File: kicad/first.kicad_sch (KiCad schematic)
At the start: 100 parts, among them J1 Conn_01x04_Pin, P1 USB_C_Plug_USB2.0, Q1 MMUN2111LT1G, Q2 MMBT3904, Q3 MMUN2111LT1G, Q4 MMBT3904, SW1 SW_SPDT, SW2 RotaryEncoder_Switch_MP, SW3 RotaryEncoder_Switch_MP, SW4 RotaryEncoder_Switch_MP, U1 OPA1678, U1 STM32F407VETx, U2 OPA1678, U3 CS4272, U3 OPA1678, U4 TPS7A20xxxDBV, Y1 16 MHz

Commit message: um
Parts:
- removed C20: 47u, symbol Device:C
- added C20: 47u, symbol Device:C_Polarized
- added C44: 100n/50V+, symbol Device:C
- C14: value 1u -> 1u /10V
- C15: value 1u -> 1u/10V
- C22: value 1u -> 1u/10V+
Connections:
- net GND: now also C20.2, C44.2
- net VQ1: now also C44.1
- net at C21.1, U3.22 (FILT+): now also C20.1
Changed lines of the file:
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@@
 	)
 	(junction
+		(at 372.11 140.97)
+		(diameter 0)
+		(color 0 0 0 0)
+	)
+	(junction
 		(at 181.61 33.02)
 		(diameter 0)
@@
 	)
 	(junction
-		(at 349.25 143.51)
-		(diameter 0)
-		(color 0 0 0 0)
-	)
-	(junction
 		(at 121.92 114.3)
 		(diameter 0)
@@
 	)
 	(junction
+		(at 349.25 143.51)
+		(diameter 0)
+		(color 0 0 0 0)
+	)
+	(junction
 		(at 300.99 83.82)
 		(diameter 0)
@@
 	(wire
 		(pts
+			(xy 372.11 140.97) (xy 387.35 140.97)
+		)
+		(stroke
+			(width 0)
+			(type default)
+		)
+	)
+	(wire
+		(pts
 			(xy 158.75 271.78) (xy 158.75 273.05)
 		)
@@
 	(wire
 		(pts
+			(xy 387.35 142.24) (xy 387.35 140.97)
+		)
+		(stroke
+			(width 0)
+			(type default)
+		)
+	)
+	(wire
+		(pts
 			(xy 229.87 181.61) (xy 229.87 182.88)
 		)
@@
 	(wire
 		(pts
+			(xy 387.35 149.86) (xy 387.35 151.13)
+		)
+		(stroke
+			(width 0)
+			(type default)
+		)
+	)
+	(wire
+		(pts
 			(xy 336.55 223.52) (xy 328.93 223.52)
 		)
@@
 	(wire
 		(pts
+			(xy 387.35 151.13) (xy 372.11 151.13)
+		)
+		(stroke
+			(width 0)
+			(type default)
+		)
+	)
+	(wire
+		(pts
 			(xy 269.24 234.95) (xy 293.37 234.95)
 		)
@@
 	(wire
 		(pts
-			(xy 349.25 143.51) (xy 360.68 143.51)
-		)
-		(stroke
-			(width 0)
-			(type default)
-		)
-	)
-	(wire
-		(pts
 			(xy 300.99 148.59) (xy 304.8 148.59)
 		)
@@
 	(wire
 		(pts
+			(xy 349.25 143.51) (xy 360.68 143.51)
+		)
+		(stroke
+			(width 0)
+			(type default)
+		)
+	)
+	(wire
+		(pts
 			(xy 293.37 234.95) (xy 321.31 234.95)
 		)
@@
 	(symbol
 		(lib_id "Device:C")
+		(at 387.35 146.05 0)
+		(unit 1)
+		(body_style 1)
+		(exclude_from_sim no)
+		(in_bom yes)
+		(on_board yes)
+		(in_pos_files yes)
+		(dnp no)
+		(fields_autoplaced yes)
+		(property "Reference" "C44"
+			(at 391.16 144.7799 0)
+			(show_name no)
+			(do_not_autoplace no)
+			(effects
+				(font
+					(size 1.27 1.27)
+				)
+				(justify left)
+			)
+		)
+		(property "Value" "100n/50V+"
+			(at 391.16 147.3199 0)
+			(show_name no)
+			(do_not_autoplace no)
+			(effects
+				(font
+					(size 1.27 1.27)
+				)
+				(justify left)
+			)
+		)
+		(property "Footprint" ""
+			(at 388.3152 149.86 0)
+			(hide yes)
+			(show_name no)
+			(do_not_autoplace no)
+			(effects
+				(font
+					(size 1.27 1.27)
+				)
+			)
+		)
+		(property "Datasheet" ""
+			(at 387.35 146.05 0)
+			(hide yes)
+			(show_name no)
+			(do_not_autoplace no)
+			(effects
+				(font
+					(size 1.27 1.27)
+				)
+			)
+		)
+		(property "Description" "Unpolarized capacitor"
+			(at 387.35 146.05 0)
+			(hide yes)
+			(show_name no)
+			(do_not_autoplace no)
+			(effects
+				(font
+					(size 1.27 1.27)
+				)
+			)
+		)
+		(pin "1"
+		)
+		(pin "2"
+		)
+		(instances
+			(project "first"
+				(path "/580becc7-fa47-4b4d-a43e-4b9316967eb7"
+					(reference "C44")
+					(unit 1)
+				)
+			)
+		)
+	)
+	(symbol
+		(lib_id "Device:C")
 		(at 59.69 261.62 270)
 		(unit 1)
@@
 			)
 		)
-		(property "Value" "1u"
+		(property "Value" "1u /10V"
 			(at 326.898 34.036 0)
 			(show_name no)
@@
 	)
 	(symbol
+		(lib_id "Device:C_Polarized")
+		(at 349.25 147.32 0)
+		(unit 1)
+		(body_style 1)
+		(exclude_from_sim no)
+		(in_bom yes)
+		(on_board yes)
+		(in_pos_files yes)
+		(dnp no)
+		(fields_autoplaced yes)
+		(property "Reference" "C20"
+			(at 353.06 145.1609 0)
+			(show_name no)
+			(do_not_autoplace no)
+			(effects
+				(font
+					(size 1.27 1.27)
+				)
+				(justify left)
+			)
+		)
+		(property "Value" "47u"
+			(at 353.06 147.7009 0)
+			(show_name no)
+			(do_not_autoplace no)
+			(effects
+				(font
+					(size 1.27 1.27)
+				)
+				(justify left)
+			)
+		)
+		(property "Footprint" ""
+			(at 350.2152 151.13 0)
+			(hide yes)
+			(show_name no)
+			(do_not_autoplace no)
+			(effects
+				(font
+					(size 1.27 1.27)
+				)
+			)
+		)
+		(property "Datasheet" ""
+			(at 349.25 147.32 0)
+			(hide yes)
+			(show_name no)
+			(do_not_autoplace no)
+			(effects
+				(font
+					(size 1.27 1.27)
+				)
+			)
+		)
+		(property "Description" "Polarized capacitor"
+			(at 349.25 147.32 0)
+			(hide yes)
+			(show_name no)
+			(do_not_autoplace no)
+			(effects
+				(font
+					(size 1.27 1.27)
+				)
+			)
+		)
+		(pin "1"
+		)
+		(pin "2"
+		)
+		(instances
+			(project "first"
+				(path "/580becc7-fa47-4b4d-a43e-4b9316967eb7"
+					(reference "C20")
+					(unit 1)
+				)
+			)
+		)
+	)
+	(symbol
 		(lib_id "Amplifier_Operational:NE5532")
 		(at 87.63 240.03 0)
@@
 			)
 		)
-		(property "Value" "1u"
+		(property "Value" "1u/10V"
 			(at 358.14 33.0199 0)
 			(show_name no)
@@
 	)
 	(symbol
-		(lib_id "Device:C")
-		(at 349.25 147.32 0)
-		(unit 1)
-		(body_style 1)
-		(exclude_from_sim no)
-		(in_bom yes)
-		(on_board yes)
-		(in_pos_files yes)
-		(dnp no)
-		(fields_autoplaced yes)
-		(property "Reference" "C20"
-			(at 353.06 146.0499 0)
-			(show_name no)
-			(do_not_autoplace no)
-			(effects
-				(font
-					(size 1.27 1.27)
-				)
-				(justify left)
-			)
-		)
-		(property "Value" "47u"
-			(at 353.06 148.5899 0)
-			(show_name no)
-			(do_not_autoplace no)
-			(effects
-				(font
-					(size 1.27 1.27)
-				)
-				(justify left)
-			)
-		)
-		(property "Footprint" ""
-			(at 350.2152 151.13 0)
-			(hide yes)
-			(show_name no)
-			(do_not_autoplace no)
-			(effects
-				(font
-					(size 1.27 1.27)
-				)
-			)
-		)
-		(property "Datasheet" ""
-			(at 349.25 147.32 0)
-			(hide yes)
-			(show_name no)
-			(do_not_autoplace no)
-			(effects
-				(font
-					(size 1.27 1.27)
-				)
-			)
-		)
-		(property "Description" "Unpolarized capacitor"
-			(at 349.25 147.32 0)
-			(hide yes)
-			(show_name no)
-			(do_not_autoplace no)
-			(effects
-				(font
-					(size 1.27 1.27)
-				)
-			)
-		)
-		(pin "2"
-		)
-		(pin "1"
-		)
-		(instances
-			(project "first"
-				(path "/580becc7-fa47-4b4d-a43e-4b9316967eb7"
-					(reference "C20")
-					(unit 1)
-				)
-			)
-		)
-	)
-	(symbol
 		(lib_id "Connector:Conn_01x04_Pin")
 		(at 302.26 99.06 0)
@@
 			)
 		)
-		(property "Value" "1u"
+		(property "Value" "1u/10V+"
 			(at 375.92 147.3199 0)
 			(show_name no)

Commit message: some cleanup, output audio connectors, some capacitor changes at input buffer and preamp
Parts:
- removed C23, C24: 10u, symbol Device:C_Polarized
- added C24, C25: 47n, symbol Device:C
- C23: renamed from C44; value 100n/50V+ -> 100n
- renumbered C25 to C26, C26 to C27, C27 to C28, C28 to C29, C29 to C30, C30 to C31, C31 to C32, C32 to C33, C33 to C34, C34 to C35, C35 to C36, C36 to C37, C37 to C38, C38 to C39, C39 to C40, C40 to C41
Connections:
- net Inputs/AIN_L: now also C24.2
- net Inputs/AIN_R: now also C25.2
- net at R5.2, U1.5 (+): now also C25.1
- net at R4.1, U1.3 (+): now also C24.1
- net AOUTA renamed AOUT_L
- net AOUTB renamed AOUT_R

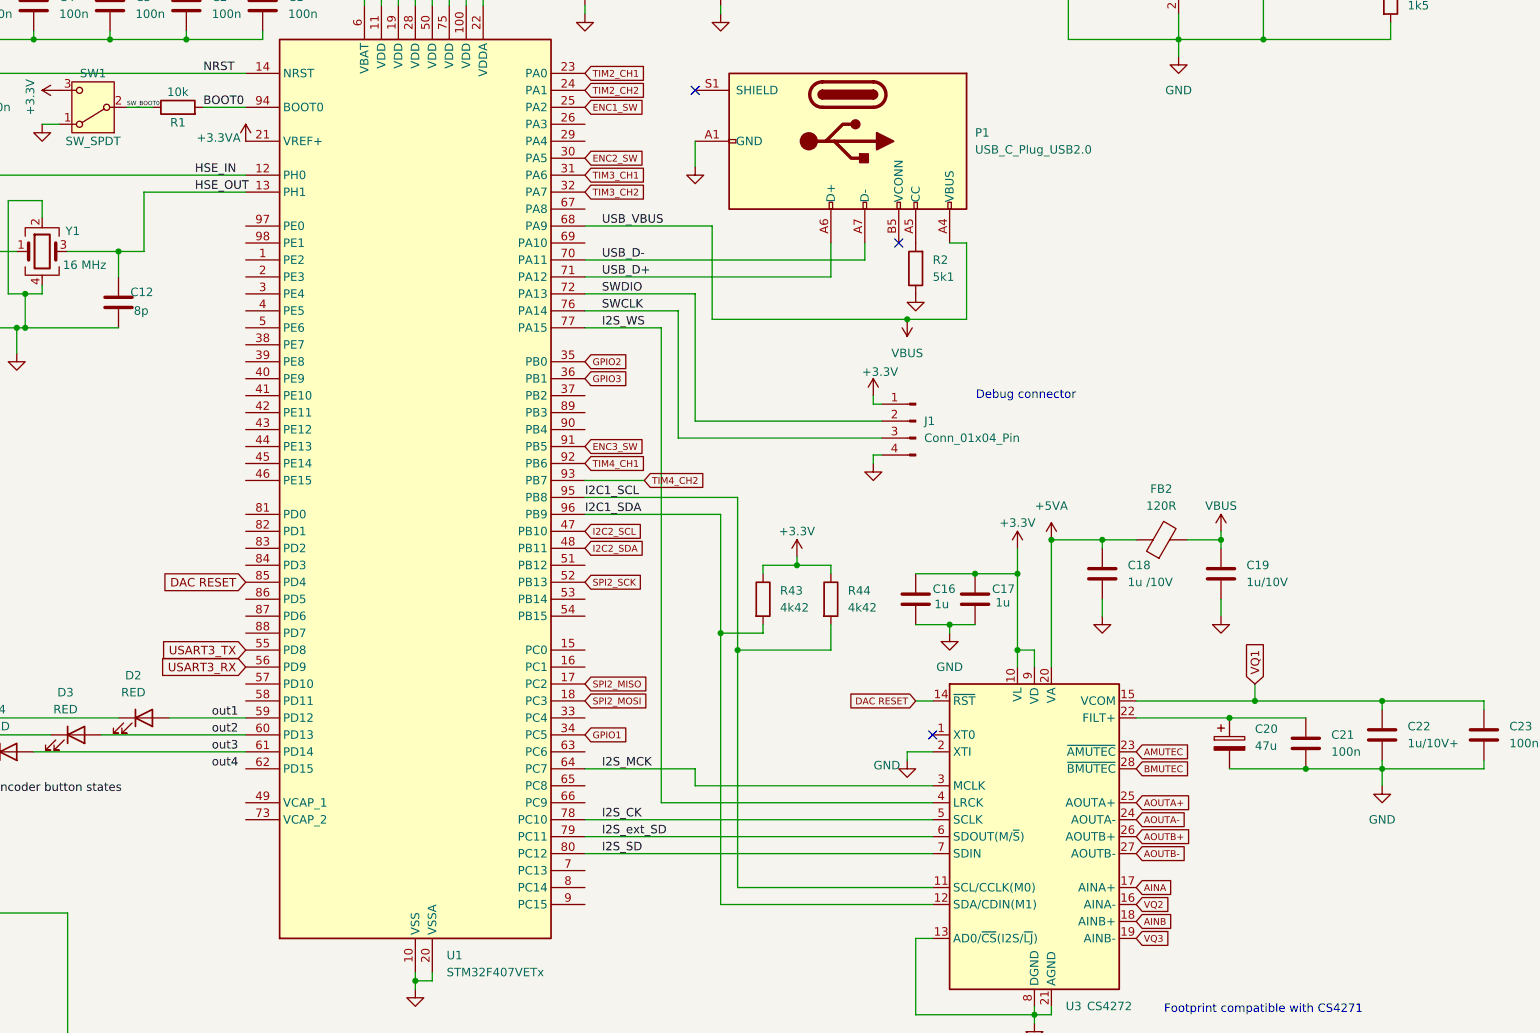
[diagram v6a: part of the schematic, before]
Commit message: extra pin header, VCAP capacitors, no connect flags
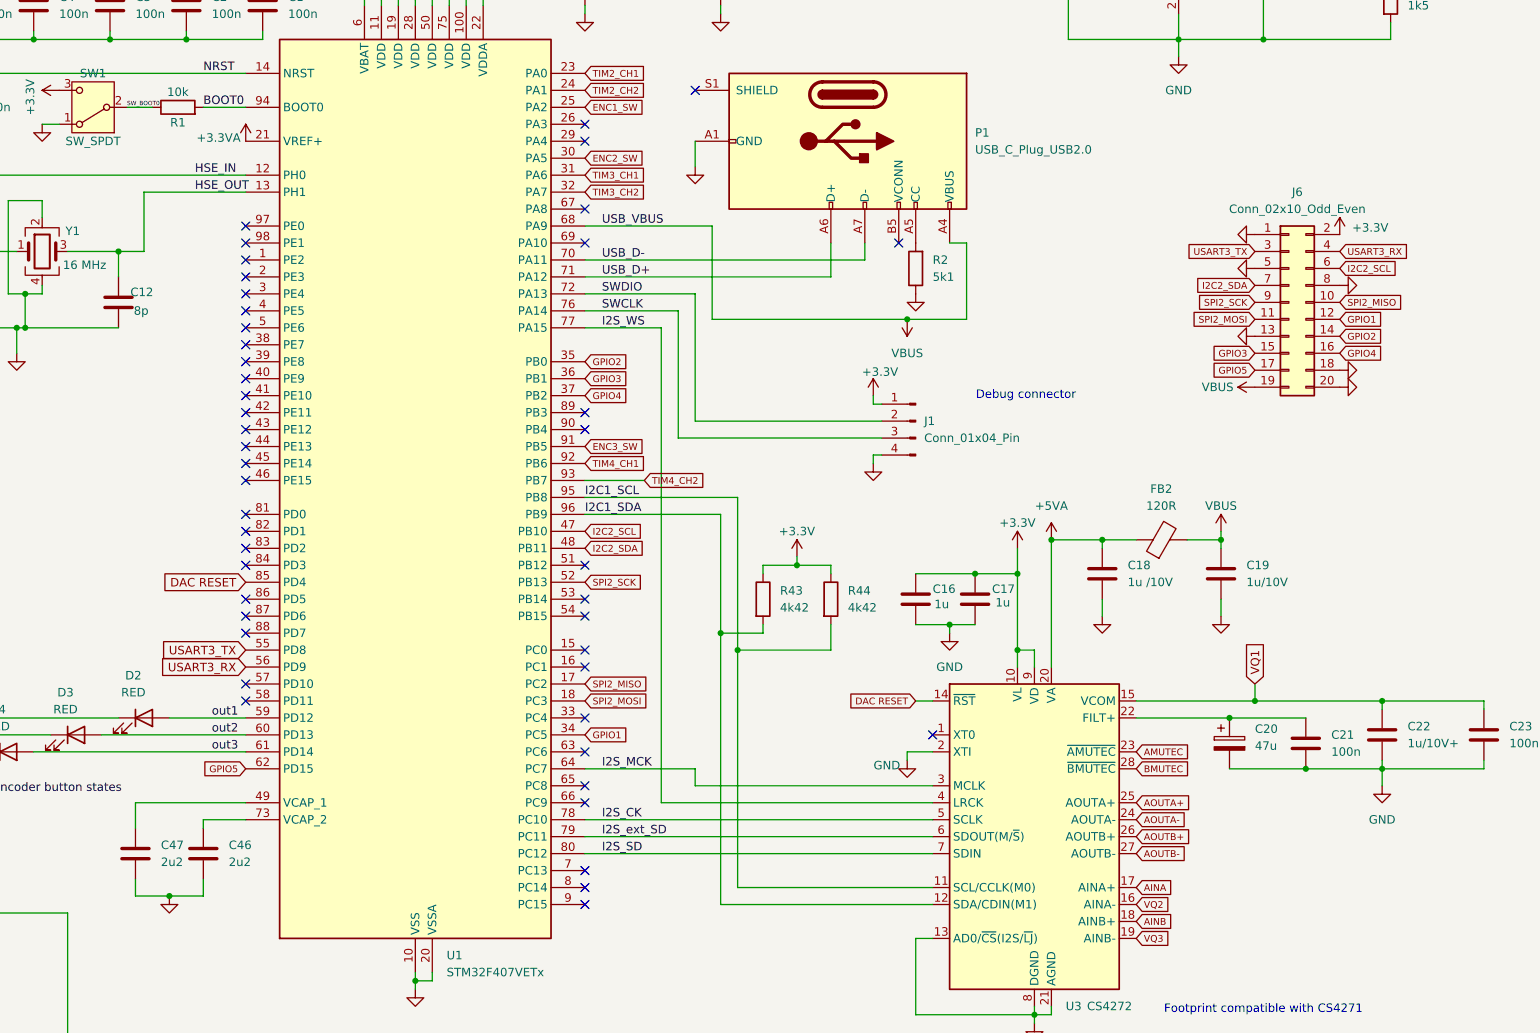
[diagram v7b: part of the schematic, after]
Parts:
- added C46, C47: 2u2, symbol Device:C
- added J6: Conn_02x10_Odd_Even, Connector_PinHeader_2.54mm:PinHeader_2x10_P2.54mm_Vertical, symbol Connector_Generic:Conn_02x10_Odd_Even
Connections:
- net +3.3V: now also J6.2 (Pin_2)
- net GND: now also C46.1, C47.1, J6.1 (Pin_1), J6.13 (Pin_13), J6.18 (Pin_18), J6.20 (Pin_20), J6.5 (Pin_5), J6.8 (Pin_8)
- net GPIO1: now also J6.12 (Pin_12)
- net GPIO2: now also J6.14 (Pin_14)
- net GPIO3: now also J6.15 (Pin_15)
- net I2C2_SCL: now also J6.6 (Pin_6)
- net I2C2_SDA: now also J6.7 (Pin_7)
- net SPI2_MISO: now also J6.10 (Pin_10)
- net SPI2_MOSI: now also J6.11 (Pin_11)
- net SPI2_SCK: now also J6.9 (Pin_9)
- net USART3_RX: now also J6.4 (Pin_4)
- net USART3_TX: now also J6.3 (Pin_3)
- net VBUS: now also J6.19 (Pin_19)
- net GPIO4: now reaches U1.37 (PB2)
- net GPIO4: now also J6.16 (Pin_16)
- net at U1.49 (VCAP_1): now also C47.2
- net GPIO5: now reaches U1.62 (PD15)
- net GPIO5: now also J6.17 (Pin_17)
- net at U1.73 (VCAP_2): now also C46.2
- no-connect marks 3 -> 46

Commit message: separated into 3 sheets, new usb connector + protection, ERC ok, BOM consolidation
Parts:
- removed C24, C25: 47n, symbol Device:C
- removed C26, C27, C32, C38: 470p, symbol Device:C
- removed C28, C29: 2700p, symbol Device:C
- removed C30, C36: 2200p, symbol Device:C
- removed C31, C37: 6800p, symbol Device:C
- removed C33, C39: 1n5, symbol Device:C
- removed C34, C35, C40, C41: 22u, symbol Device:C_Polarized
- removed J6: Conn_02x10_Odd_Even, Connector_PinHeader_2.54mm:PinHeader_2x10_P2.54mm_Vertical, symbol Connector_Generic:Conn_02x10_Odd_Even
- removed P1: USB_C_Plug_USB2.0, symbol Connector:USB_C_Plug_USB2.0
- removed Q1, Q3: MMUN2111LT1G, easyeda2kicad:SOT-23-3_L2.9-W1.3-P1.90-LS2.4-BR, symbol easyeda2kicad:MMUN2111LT1G
- removed Q2, Q4: MMBT3904, Package_TO_SOT_SMD:SOT-23, symbol Transistor_BJT:MMBT3904
- removed R10, R18: 4k42, symbol Device:R
- removed R11, R21: 2k32, symbol Device:R
- removed R12, R22: 715, symbol Device:R
- removed R13, R19: 1k33, symbol Device:R
- removed R14, R20: 1k5, symbol Device:R
- removed R15, R24: 560, symbol Device:R
- removed R16, R25: 47k, symbol Device:R
- removed R17, R23: 4k99, symbol Device:R
- removed R26, R28: 10k, symbol Device:R
- removed R27, R29: 2k, symbol Device:R
- removed R4, R5: 1M, symbol Device:R
- removed R6, R8: 634, symbol Device:R
- removed R7, R9: 91, symbol Device:R
- removed unit 2 of U1
- removed U2, U3: OPA1678, Package_SO:SOIC-8_3.9x4.9mm_P1.27mm, symbol Amplifier_Operational:NE5532
- removed unit 2 of U3
- removed Y1: 16 MHz, symbol Device:Crystal_GND24
- added J2: USB_C_Receptacle_USB2.0_16P, symbol Connector:USB_C_Receptacle_USB2.0_16P
- added J6: Conn_02x08_Odd_Even, symbol Connector_Generic:Conn_02x08_Odd_Even
- added R3: 5k1, symbol Device:R
- added R44: 10k, symbol Device:R
- added U7: USBLC6-2SC6, Package_TO_SOT_SMD:SOT-23-6, symbol Power_Protection:USBLC6-2SC6
- added Y2: 16MHz, symbol Device:Crystal_GND24
- C14, C18: value 1u /10V -> 1u
- C15, C19: value 1u/10V -> 1u
- C22: value 1u/10V+ -> 1u
- renumbered R3 to R4, R43 to R42, R44 to R43, U3 to U2, U4 to U3
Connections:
- net +3.3V: now also J6.2 (Pin_2), R44.1
- net GND: now also J2.A1 (GND), J2.A12 (GND), J2.B1 (GND), J2.B12 (GND), J2.SH (SHIELD), J6.1 (Pin_1), J6.14 (Pin_14), J6.16 (Pin_16), J6.5 (Pin_5), R3.1, U7.2 (GND), Y2.2 (G), Y2.4 (G)
- net GPIO1: now also J6.9 (Pin_9), R44.2
- net GPIO2: now also J6.10 (Pin_10)
- net GPIO3: now also J6.11 (Pin_11)
- net GPIO4: now also J6.12 (Pin_12)
- net GPIO5: now also J6.13 (Pin_13)
- net HSE_IN: now also Y2.1
- net HSE_OUT: now also Y2.3
- net SPI2_MISO: now also J6.7 (Pin_7)
- net SPI2_MOSI: now also J6.8 (Pin_8)
- net SPI2_SCK: now also J6.6 (Pin_6)
- net USART3_RX: now also J6.4 (Pin_4)
- net USART3_TX: now also J6.3 (Pin_3)
- net USB_D+: now also U7.4 (I/O2)
- net USB_D-: now also U7.6 (I/O1)
- net VBUS: now also J2.A4 (VBUS), J2.A9 (VBUS), J2.B4 (VBUS), J2.B9 (VBUS), J6.15 (Pin_15), U7.5 (VBUS); no longer U1.68 (PA9)
- net at R2.2: now also J2.A5 (CC1)
- net I2C2_SCL: no longer names the net of U1.47 (PB10)
- net I2C2_SDA: no longer names the net of U1.48 (PB11)
- net VQ2 renamed VQ23
- new net: J2.A6 (D+), J2.B6 (D+), U7.3 (I/O2)
- new net: J2.A7 (D-), J2.B7 (D-), U7.1 (I/O1)
- new net: J2.B5 (CC2), R3.2
- no-connect marks 46 -> 52
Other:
- removed sheet Inputs
- note added: "External interfaces"
- note added: "These correspond to the button states"
- note removed: "Analog input buffer"
- note removed: "Analog output filters"
- note removed: "Mute circuits"
- moved on the sheet: C1, C10, C11, C12, C13, C14, C15, C16, C17, C18, C19, C2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
